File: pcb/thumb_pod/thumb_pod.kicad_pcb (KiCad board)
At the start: 2 copper layers, 93 x 56 mm, 54 parts, among them J1 Conn_02x06_Odd_Even, J2 Conn_02x06_Odd_Even, J3 Conn_02x06_Odd_Even, SW1 SW_Push, SW10 SW_Push, SW2 SW_Push, SW3 SW_Push, SW4 SW_Push, SW5 SW_Push, SW6 SW_Push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

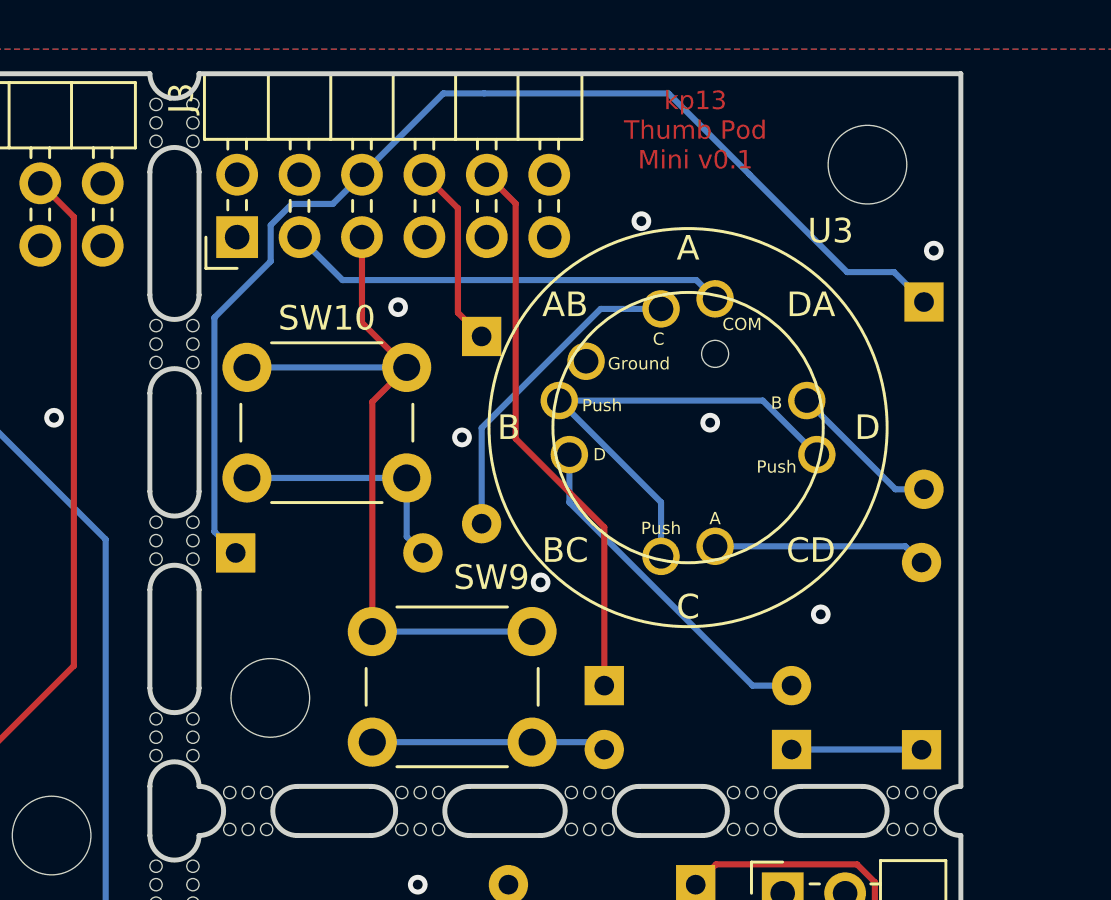
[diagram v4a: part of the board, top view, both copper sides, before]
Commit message: - Updated the "mini" thumb pod with an angled PCB edge
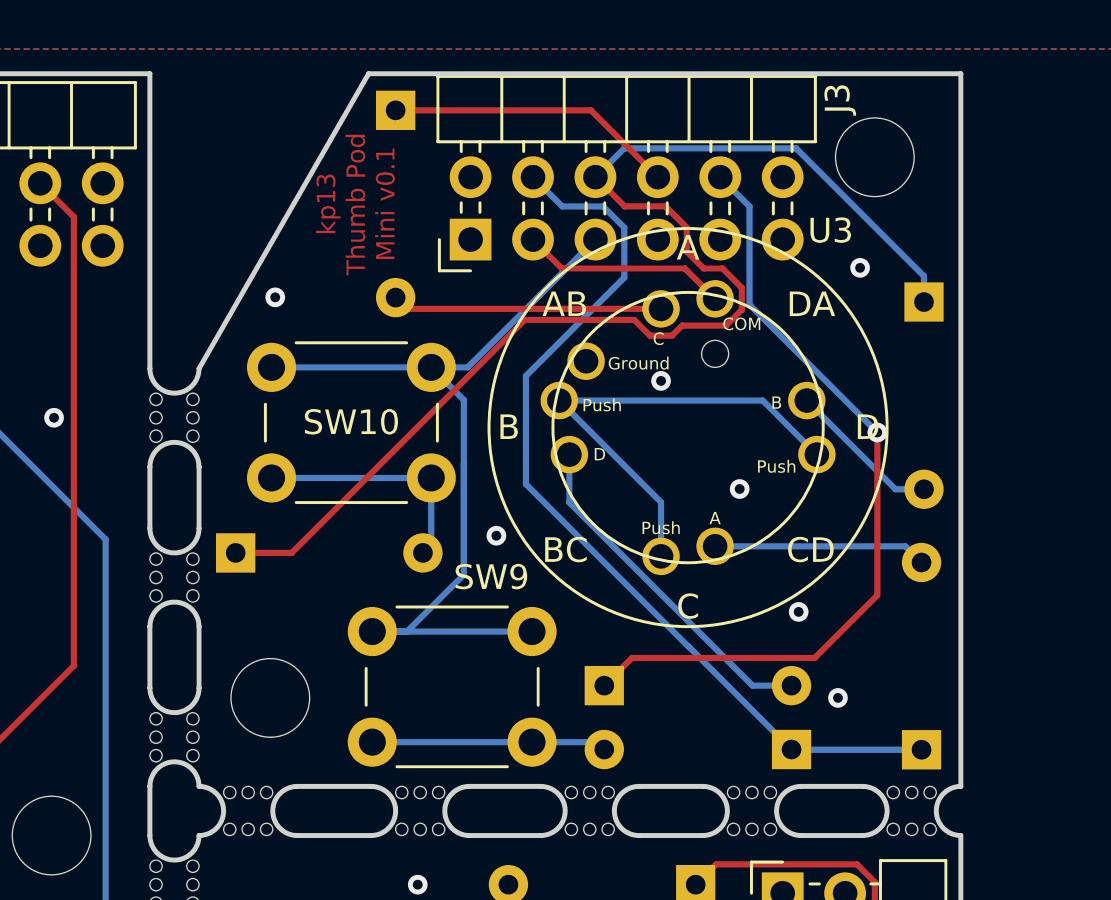
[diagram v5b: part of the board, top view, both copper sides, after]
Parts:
- removed the mouse-bite-2mm-slot at (147.0, 43.0)
- removed the mouse-bite-2mm-slot at (147.0, 26.0)
- added mouse-bite-2mm-slot: VAL**, thumb_pod:mouse-bite-2mm-slot, F.Cu at (147.0, 44.5)
- moved D15 9.84 mm to (156.0, 25.5)
- moved J3 9.50 mm to (159.1, 30.8)
- moved mouse-bite-2mm-slot 3.00 mm to (147.0, 38.0)
- moved SW10 1.00 mm to (150.9, 36.0)
- moved H7 0.42 mm to (175.5, 27.4)
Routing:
- net /Col0: track 50.5 -> 82.5 mm
- net /Row4: track 46.2 -> 36.7 mm
- net /Col3: track 80.7 -> 90.2 mm, vias 0 -> 1
- net /Row5: track 154.8 -> 164.0 mm
- net /Col1: track 120.7 -> 125.3 mm
- net /Col2: track 40.7 -> 44.9 mm
- net Net-(D15-Pad2): track 13.2 -> 11.0 mm
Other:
- outline, holes or cut-outs redrawn

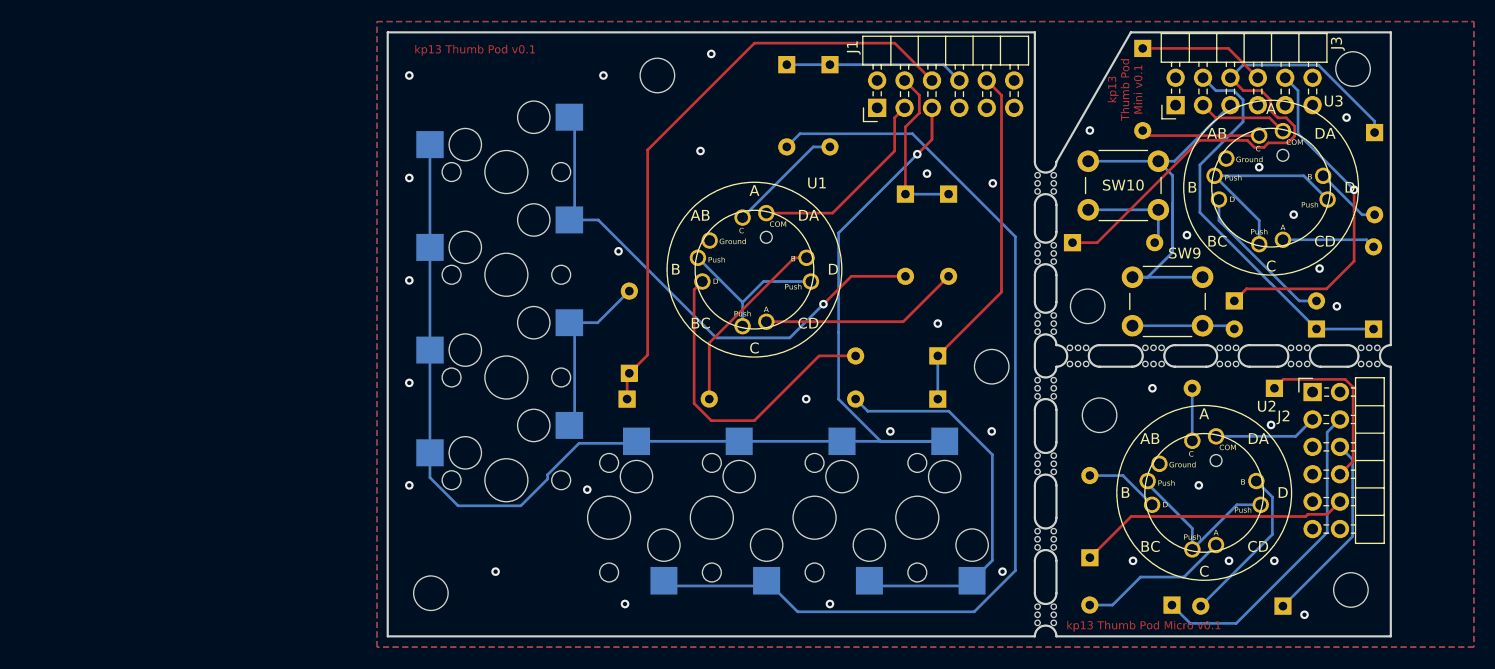
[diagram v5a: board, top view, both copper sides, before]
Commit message: - Rearranged sub-boards to (hopefully) make manufacturing easier  - Fixed the schematic to better isolate each thumb pod version
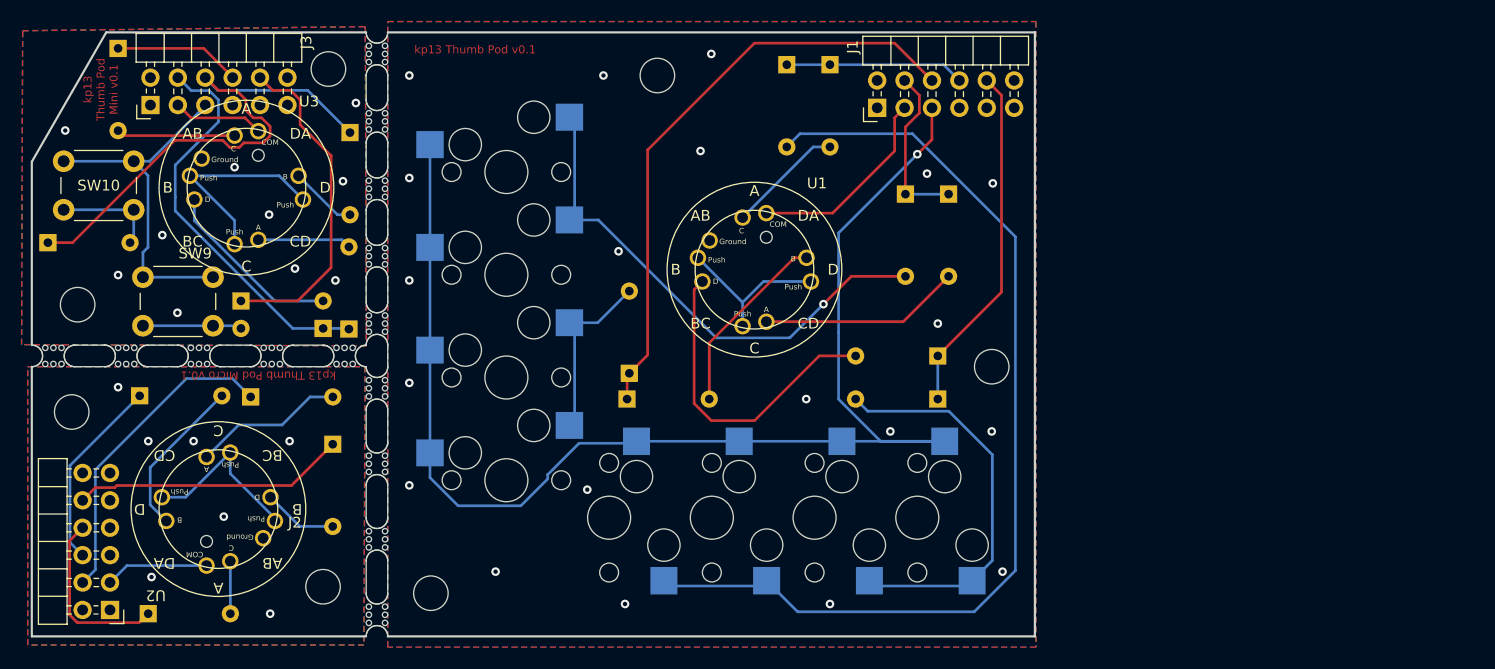
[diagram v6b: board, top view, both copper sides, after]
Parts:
- removed the mouse-bite-2mm-slot at (177.0, 54.0)
- removed the mouse-bite-2mm-slot at (170.5, 54.0)
- removed the mouse-bite-2mm-slot at (147.0, 57.0)
- removed the mouse-bite-2mm-slot at (147.0, 71.0)
- removed the mouse-bite-2mm-slot at (147.0, 64.0)
- removed the mouse-bite-2mm-slot at (163.9, 54.0)
- removed the mouse-bite-2mm-slot at (157.0, 54.0)
- removed the mouse-bite-2mm-slot at (147.0, 51.0)
- removed the mouse-bite-2mm-slot at (147.0, 78.0)
- removed the mouse-bite-2mm-slot at (150.0, 54.0)
- removed the mouse-bite-2mm-slot at (147.0, 44.5)
- removed the mouse-bite-2mm-slot at (147.0, 38.0)
- added mouse-bite-2mm-slot: VAL**, thumb_pod:mouse-bite-2mm-slot, F.Cu at (61.8, 54.0)
- added mouse-bite-2mm-slot: VAL**, thumb_pod:mouse-bite-2mm-slot, F.Cu at (85.0, 32.2)
- added mouse-bite-2mm-slot: VAL**, thumb_pod:mouse-bite-2mm-slot, F.Cu at (85.0, 57.0)
- added mouse-bite-2mm-slot: VAL**, thumb_pod:mouse-bite-2mm-slot, F.Cu at (85.0, 64.0)
- added mouse-bite-2mm-slot: VAL**, thumb_pod:mouse-bite-2mm-slot, F.Cu at (82.0, 54.0)
- added mouse-bite-2mm-slot: VAL**, thumb_pod:mouse-bite-2mm-slot, F.Cu at (85.0, 26.0)
- added mouse-bite-2mm-slot: VAL**, thumb_pod:mouse-bite-2mm-slot, F.Cu at (85.0, 78.0)
- added mouse-bite-2mm-slot: VAL**, thumb_pod:mouse-bite-2mm-slot, F.Cu at (85.0, 38.5)
- added mouse-bite-2mm-slot: VAL**, thumb_pod:mouse-bite-2mm-slot, F.Cu at (85.0, 71.0)
- added mouse-bite-2mm-slot: VAL**, thumb_pod:mouse-bite-2mm-slot, F.Cu at (55.0, 54.0)
- added mouse-bite-2mm-slot: VAL**, thumb_pod:mouse-bite-2mm-slot, F.Cu at (68.5, 54.0)
- added mouse-bite-2mm-slot: VAL**, thumb_pod:mouse-bite-2mm-slot, F.Cu at (85.0, 44.8)
- added mouse-bite-2mm-slot: VAL**, thumb_pod:mouse-bite-2mm-slot, F.Cu at (75.2, 54.0)
- added mouse-bite-2mm-slot: VAL**, thumb_pod:mouse-bite-2mm-slot, F.Cu at (85.0, 51.0)
- moved H5 119.7 mm to (56.7, 59.2), turned to 180 degrees
- moved J2 113.3 mm to (60.2, 77.5), turned to 180 degrees
- moved D10 107.8 mm to (63.0, 57.7), turned to 0 degrees
- moved D11 106.5 mm to (63.8, 77.9), turned to 0 degrees
- moved J3 95.1 mm to (64.0, 30.7)
- moved D13 95.0 mm to (82.4, 51.5)
- moved D14 95.0 mm to (82.5, 33.3)
- moved D15 95.0 mm to (61.0, 25.5)
- moved D18 95.0 mm to (54.5, 43.5)
- moved H7 95.0 mm to (80.5, 27.4)
- moved U3 95.0 mm to (72.9, 38.4)
- moved SW10 95.0 mm to (56.0, 36.0)
- moved H6 93.7 mm to (57.2, 49.2)
- moved D16 92.1 mm to (80.0, 51.5)
- moved D17 92.1 mm to (72.4, 48.9)
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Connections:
- D10 pad 1: /Col1 -> Net-(J2-Pad6)
- D11 pad 1: /Col2 -> Net-(J2-Pad8)
- D12 pad 1: /Col3 -> Net-(J2-Pad10)
- D13 pad 1: /Col0 -> Net-(D13-Pad1)
- D14 pad 1: /Col1 -> Net-(D14-Pad1)
- D15 pad 1: /Col2 -> Net-(J3-Pad8)
- D16 pad 1: /Col0 -> Net-(D13-Pad1)
- D17 pad 1: /Col3 -> Net-(D17-Pad1)
- D18 pad 1: /Col1 -> Net-(D14-Pad1)
- D9 pad 1: /Col0 -> Net-(J2-Pad4)
- J2 pad 1: /GND -> /GND_u
- J2 pad 10: /Col3 -> Net-(J2-Pad10)
- J2 pad 11: /Col5 -> unconnected-(J2-Pad11)
- J2 pad 12: /Col4 -> unconnected-(J2-Pad12)
- J2 pad 2: /3.3v -> unconnected-(J2-Pad2)
- J2 pad 3: /Row4 -> Net-(J2-Pad3)
- J2 pad 4: /Col0 -> Net-(J2-Pad4)
- J2 pad 5: /Row5 -> unconnected-(J2-Pad5)
- J2 pad 6: /Col1 -> Net-(J2-Pad6)
- J2 pad 8: /Col2 -> Net-(J2-Pad8)
- J3 pad 1: /GND -> /GND_m
- J3 pad 10: /Col3 -> Net-(D17-Pad1)
- J3 pad 11: /Col5 -> unconnected-(J3-Pad11)
- J3 pad 12: /Col4 -> unconnected-(J3-Pad12)
- J3 pad 2: /3.3v -> unconnected-(J3-Pad2)
- J3 pad 3: /Row4 -> Net-(J3-Pad3)
- J3 pad 4: /Col0 -> Net-(D13-Pad1)
- J3 pad 5: /Row5 -> Net-(J3-Pad5)
- J3 pad 6: /Col1 -> Net-(D14-Pad1)
- J3 pad 8: /Col2 -> Net-(J3-Pad8)
- SW10 pad 1: /Row5 -> Net-(J3-Pad5)
- SW9 pad 1: /Row5 -> Net-(J3-Pad5)
- U2 pad 1: /Row4 -> Net-(J2-Pad3)
- U2 pad 6: /GND -> /GND_u
- U3 pad 1: /Row4 -> Net-(J3-Pad3)
- U3 pad 6: /GND -> /GND_m
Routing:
- net /Col1: track 125.3 -> 55.8 mm
- net /Col0: track 82.5 -> 15.6 mm
- net /Col3: track 90.2 -> 32.6 mm, vias 1 -> 0
- net Net-(D14-Pad1): track 0.00 -> 50.0 mm
- net /Row5: track 164.0 -> 124.4 mm
- net Net-(D13-Pad1): track 0.00 -> 37.2 mm
- net Net-(J3-Pad5): track 0.00 -> 33.3 mm
- net Net-(D17-Pad1): track 0.00 -> 30.9 mm
- net Net-(J2-Pad4): track 0.00 -> 29.6 mm
- net /Col2: track 44.9 -> 16.6 mm
- net Net-(J2-Pad10): track 0.00 -> 25.3 mm
- net /Row4: track 36.7 -> 18.7 mm
- net Net-(J2-Pad6): track 0.00 -> 17.9 mm
- net Net-(J2-Pad8): track 0.00 -> 16.5 mm
- net Net-(J3-Pad8): track 0.00 -> 11.8 mm
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- added copper zone on B.Cu, net /GND_m
- added copper zone on F.Cu, net /GND_m
- added copper zone on B.Cu, net /GND_u
- added copper zone on F.Cu, net /GND_u
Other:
- outline, holes or cut-outs redrawn
- board text added: "Conn_02x06_Odd_Even"
- board text added: "MountingHole"
